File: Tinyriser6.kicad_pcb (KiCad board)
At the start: 4 copper layers, 113.2 x 23.5 mm, 25 parts, among them J1 Bus_M.2_Socket_M, J2 Bus_PCI_Express_x16, J3 Conn_02x04_Odd_Even, J6 USB_A, J7 Conn_01x26_Pin, M1 Fan_4pin

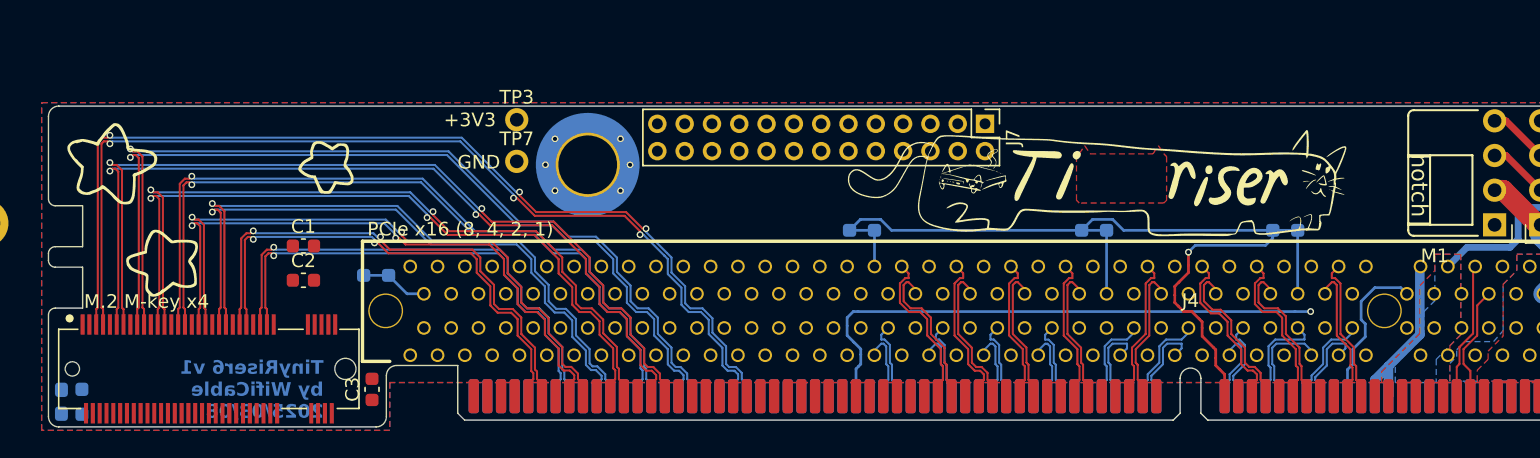
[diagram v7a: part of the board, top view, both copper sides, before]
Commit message: routed M.2 power
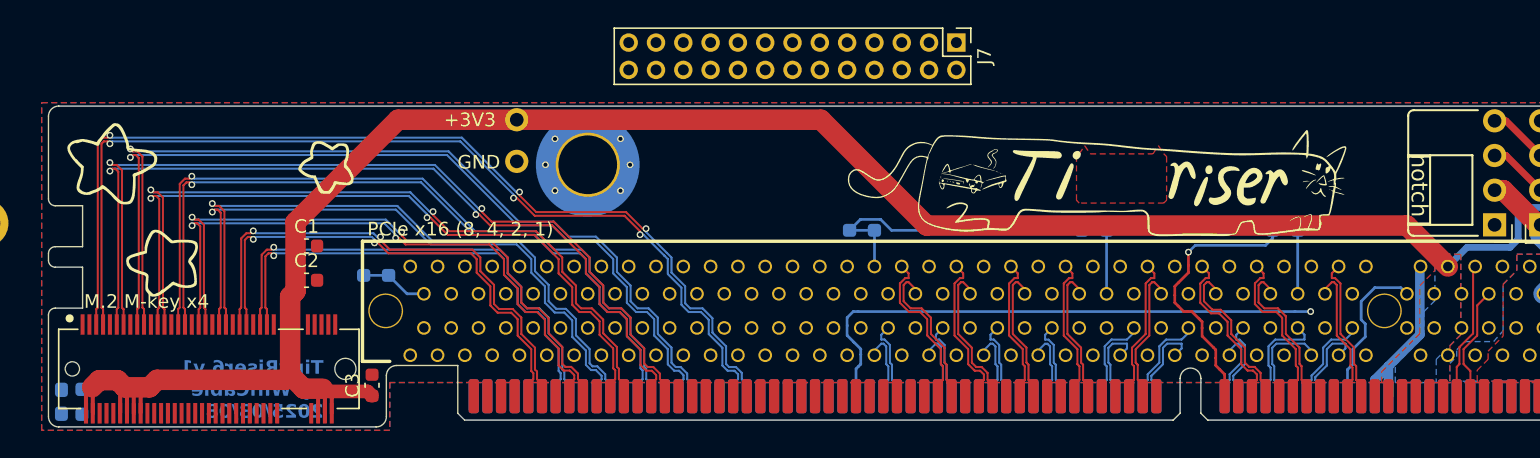
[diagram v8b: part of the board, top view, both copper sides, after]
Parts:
- moved J7 6.31 mm to (187.8, 58.1)
- moved C3 0.30 mm to (144.9, 83.2)
- moved C1 0.22 mm to (140.2, 73.0)
- moved C2 0.22 mm to (140.2, 75.5)
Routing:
- net +3V3: track 12.8 -> 153.3 mm
